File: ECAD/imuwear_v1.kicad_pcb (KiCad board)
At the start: 2 copper layers, 14 parts, among them P1 CONN_6, P2 CONN_6, U1 MPU_9150

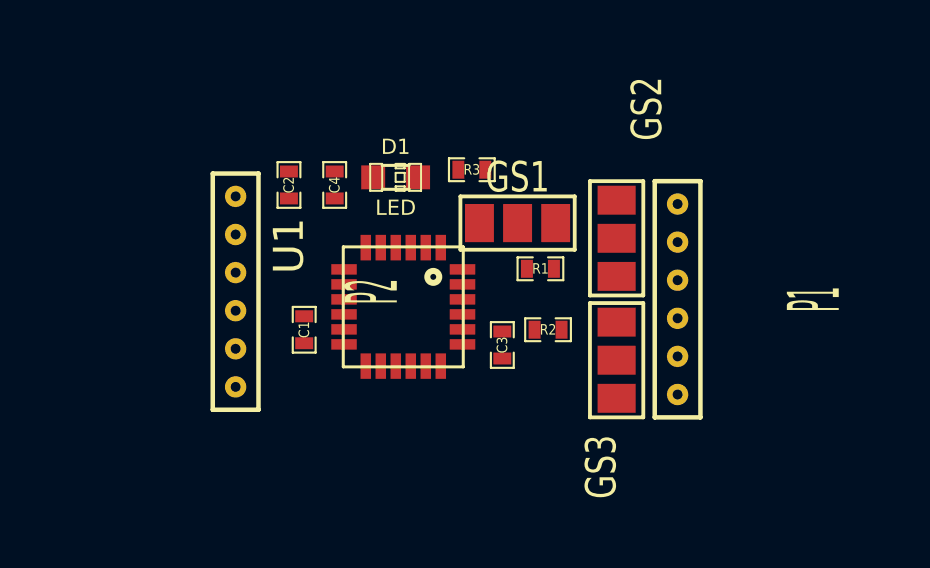
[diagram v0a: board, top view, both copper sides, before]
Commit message: Initial layout before routing PCB
board is 16.5mm x 9mm
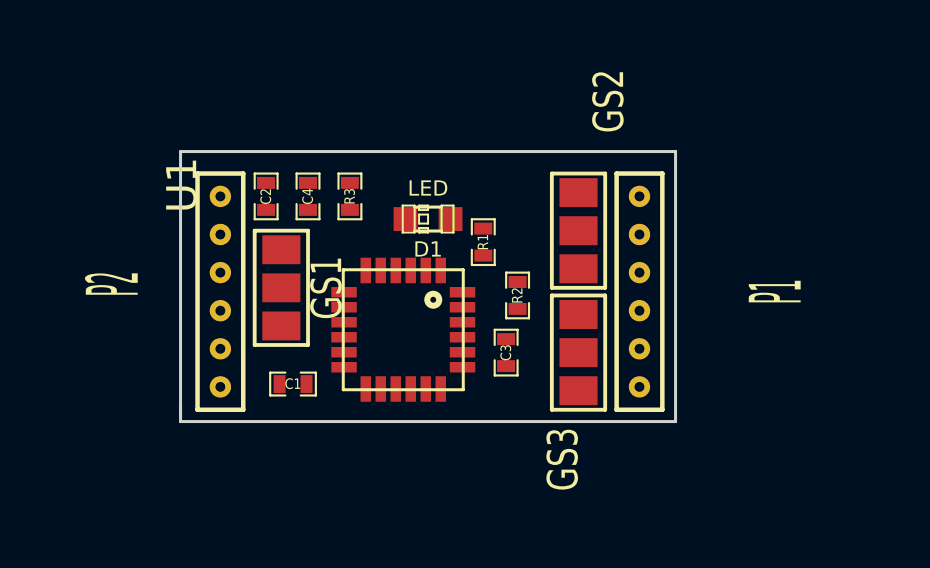
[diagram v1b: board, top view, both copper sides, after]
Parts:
- moved GS1 8.16 mm to (213.4, 153.5), turned to 0 degrees
- moved R3 4.16 mm to (215.6, 150.5), turned to 270 degrees
- moved R1 2.10 mm to (220.1, 152.0), turned to 270 degrees
- moved C1 1.85 mm to (213.8, 156.8), turned to 180 degrees
- moved D1 1.76 mm to (218.2, 151.2), turned to 180 degrees
- moved R2 1.53 mm to (221.2, 153.8), turned to 270 degrees
- moved P1 1.30 mm to (225.3, 153.7)
- moved GS2 1.30 mm to (223.3, 151.6)
- moved GS3 1.30 mm to (223.3, 155.7)
- moved C4 0.97 mm to (214.2, 150.5)
- moved C2 0.85 mm to (212.9, 150.5)
- moved U1 0.76 mm to (217.4, 154.9)
- moved P2 0.51 mm to (211.3, 153.7)
- moved C3 0.28 mm to (220.9, 155.7), turned to 90 degrees
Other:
- board outline added: 16.5 x 9 mm
- net class Default: clearance 0.254 -> 0.381; trace_width 0.254 -> 0.1524
- net class Power added: clearance 0.381, trace_width 0.3048, via_dia 0.889, via_drill 0.635
- rule trace_clearance: 0.254 -> 0.381
- rule trace_min: 0.254 -> 0.1524

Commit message: Finished first layout
need to clean up ground plane and silkscreen
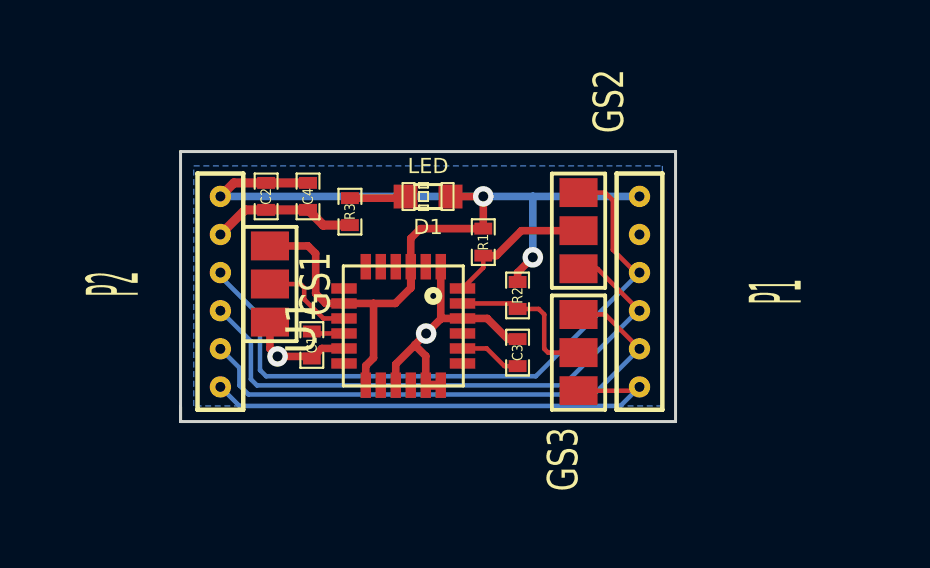
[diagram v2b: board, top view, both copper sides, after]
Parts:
- U1: footprint MPU9150 -> MPU9150_SMALL_KEEPOUT
- moved C1 1.44 mm to (214.4, 155.4), turned to 270 degrees
- moved D1 0.75 mm to (218.2, 150.5)
- moved R3 0.51 mm to (215.6, 151.0)
- moved GS1 0.40 mm to (213.0, 153.4)
- moved C3 0.38 mm to (221.2, 155.7)
- moved U1 0.13 mm to (217.4, 154.8)
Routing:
- net /VCC: track 0.00 -> 36.5 mm, vias 0 -> 2
- net /SDA1: track 0.00 -> 22.1 mm
- net /SDA2: track 0.00 -> 19.4 mm
- net /SCL1: track 0.00 -> 18.1 mm
- net GND: track 0.00 -> 17.9 mm, vias 0 -> 2
- net /SCL2: track 0.00 -> 16.6 mm
- net /SCL: track 0.00 -> 5.22 mm
- net /SDA: track 0.00 -> 4.90 mm
- net /ADDR: track 0.00 -> 3.17 mm
- net N-0000015: track 0.00 -> 2.08 mm
- net N-0000010: track 0.00 -> 1.88 mm
- net N-0000014: track 0.00 -> 1.10 mm
- added copper zone on B.Cu, net GND
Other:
- net class Default: clearance 0.381 -> 0.1524; via_dia 0.889 -> 0.6858; via_drill 0.635 -> 0.3302
- net class Power: clearance 0.381 -> 0.1524; trace_width 0.3048 -> 0.254; via_dia 0.889 -> 0.6858; via_drill 0.635 -> 0.3302
- net class Signal added: clearance 0.1524, trace_width 0.1524, via_dia 0.6858, via_drill 0.3302
- rule trace_clearance: 0.381 -> 0.1524
- rule via_min_drill: 0.508 -> 0.3302
- rule via_min_size: 0.889 -> 0.6858
